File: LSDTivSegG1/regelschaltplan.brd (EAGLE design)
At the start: 160 x 100 mm, 48 parts, among them IC3 MAX232, IC4 MEGA32-P, Q2 BSS101, Q3 BSS101, Q4 BSS101, Q5 BSS101, Q6 BSS101, Q7 BSS101, Q8 BSS101, Q9 BSS101

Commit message: edit new schaltplan
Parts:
- removed IC3/7803: (no value), v-reg:78XXS
- added C12, C13, C14, C15, C16, C17: 100n, rcl:C025-025X050
- added IC1: LF33AB, lsd2016:TO220
- added JP1: (no value), jumper:JP1
- added R10: 10K, rcl:0207/7
- added R11: 10k, rcl:0207/7
- added R12, R13, R14: 240, rcl:0207/7
- added SJ1, SJ2, SJ3, SJ4, SJ5, SJ6, SJ7, SJ8: (no value), jumper:SJ
- added SV1: (no value), con-lstb:MA05-2
- C1, C2: value (none) -> 15p
- C10, C11, C8, C9: value (none) -> 1u
- C3, C4, C6, C7: value (none) -> 100n
- C5: value (none) -> 1000u
- R1, R2, R3, R4, R5, R6, R7, R8: value (none) -> 240; device rcl:0204/7 -> rcl:0207/7
- R9: value (none) -> 10K; device rcl:0204/7 -> rcl:0207/7
- moved R5 346.2 mm to (-17.8, -426.7)
- moved R1 346.2 mm to (-17.8, -406.4)
- moved R2 346.2 mm to (-17.8, -411.5)
- moved R3 346.2 mm to (-17.8, -416.6)
- moved R4 346.2 mm to (-17.8, -421.6)
- moved R6 346.2 mm to (-17.8, -431.8)
- moved R7 346.2 mm to (-17.8, -436.9)
- moved R8 346.2 mm to (-17.8, -442.0)
- moved R9 275.3 mm to (-17.8, -467.4)
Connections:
- new net ACCEL_X: C16.1, IC4.36, U$3.3
- new net ACCEL_Y: C17.1, IC4.37, U$3.5
- new net FOOT_SW_B: IC4.29, R11.2, U$2.5
- new net GYRO_REF: C15.1, IC4.35, U$3.11
- new net GYRO_X: C13.1, IC4.33, U$3.13
- new net GYRO_Y: C14.1, IC4.34, U$3.9
- new net MISO: IC4.7, SV1.9
- new net MOSI: IC4.6, SV1.1
- new net N$19: Q9.3, SJ8.1
- new net N$30: Q8.3, SJ7.1
- new net N$31: Q7.3, SJ6.1
- new net N$34: Q4.3, SJ3.1
- new net N$35: Q3.3, SJ2.1
- new net N$45: JP1.2, X1.9
- new net N$46: LED1.K, R3.1
- new net N$47: C5.1, IC4.21, R10.1
- new net POTI: C12.1, IC4.39, U$2.2
- new net RESET: C6.2, IC4.9, R9.2, SV1.5
- new net SCK: IC4.8, SV1.7
- new net STATUS_LED1: IC4.2, LED1.A
- new net STATUS_LED2: IC4.3, LED2.A
- new net STATUS_LED3: IC4.4, LED3.A
- net +3V3: now also IC1.3, Q9.2; no longer IC3/7803.OUT
- net +5V: now also IC1.1, JP1.1, Q8.2, SJ1.2, SJ2.2, SJ3.2, SJ4.2, SJ5.2, SJ6.2, SJ7.2, SJ8.2, SV1.2; no longer IC3/7803.IN, Q2.3, Q3.3, Q4.3, Q5.3, Q6.3, Q7.3, Q8.3, Q9.3, X1.9
- net BAT_PWM: now also Q7.2, R10.2
- net DIROUT_1: now also IC4.20, Q4.2
- net DIROUT_2: now also IC4.17, Q5.2
- net ENABLE: now also IC4.24, IC4.26, Q6.2
- net GND: now also C12.2, C13.2, C14.2, C15.2, C16.2, C17.2, C5.2, IC1.2, R1.2, R11.1, R12.2, R13.2, R14.2, R2.2, R3.2, R4.2, R5.2, R6.2, R7.2, R8.2, SV1.10, SV1.4, SV1.6, SV1.8; no longer IC3/7803.GND, LED1.K, LED2.K, LED3.K, R1.1, R2.1, R3.1, R4.1, R5.1, R6.1, R7.1, R8.1
- net MOTOR_PWM1: now also IC4.19, Q2.2
- net MOTOR_PWM2: now also IC4.18, Q3.2
- net N$10: now also R5.1; no longer R2.2
- net N$11: now also R6.1; no longer R3.2
- net N$14: now also R7.1; no longer R4.2
- net N$15: now also R8.1; no longer R5.2
- net N$16: now also R12.1; no longer R6.2
- net N$17: now also R13.1; no longer R7.2
- net N$18: now also R14.1; no longer R8.2
- net N$28: now also LED2.K, R2.1; no longer U$2.5
- net N$29: now also LED3.K, R1.1; no longer U$2.2
- net N$32: now also Q6.3, SJ5.1; no longer X1.3
- net N$33: now also Q5.3, SJ4.1; no longer X1.4
- net N$4: now also Q2.3, SJ1.1; no longer C6.2, IC4.9
- net N$7: now also R4.1; no longer R1.2
- net RS232RX: now also X1.3
- net RS232TX: now also X1.4

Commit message: merge commit (maybe layout)
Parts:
- moved R14 569.9 mm to (127.0, 94.0), turned to 90 degrees
- moved R13 563.7 mm to (121.9, 94.0), turned to 90 degrees
- moved R12 557.5 mm to (116.8, 94.0), turned to 90 degrees
- moved R8 551.4 mm to (111.8, 94.0), turned to 90 degrees
- moved R7 545.3 mm to (106.7, 94.0), turned to 90 degrees
- moved R6 539.2 mm to (101.6, 94.0), turned to 90 degrees
- moved R5 533.1 mm to (96.5, 94.0), turned to 90 degrees
- moved R4 527.1 mm to (91.4, 94.0), turned to 90 degrees
- moved R3 519.1 mm to (76.2, 94.0), turned to 90 degrees
- moved R2 515.1 mm to (81.3, 94.0), turned to 90 degrees
- moved R1 511.1 mm to (86.4, 94.0), turned to 90 degrees
- moved R10 505.9 mm to (116.8, 15.2)
- moved R9 505.9 mm to (116.8, 20.3)
- moved R11 505.9 mm to (116.8, 25.4)
- moved JP1 463.8 mm to (40.6, 81.3), turned to 90 degrees
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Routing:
- added copper zone on layer 16, net GND

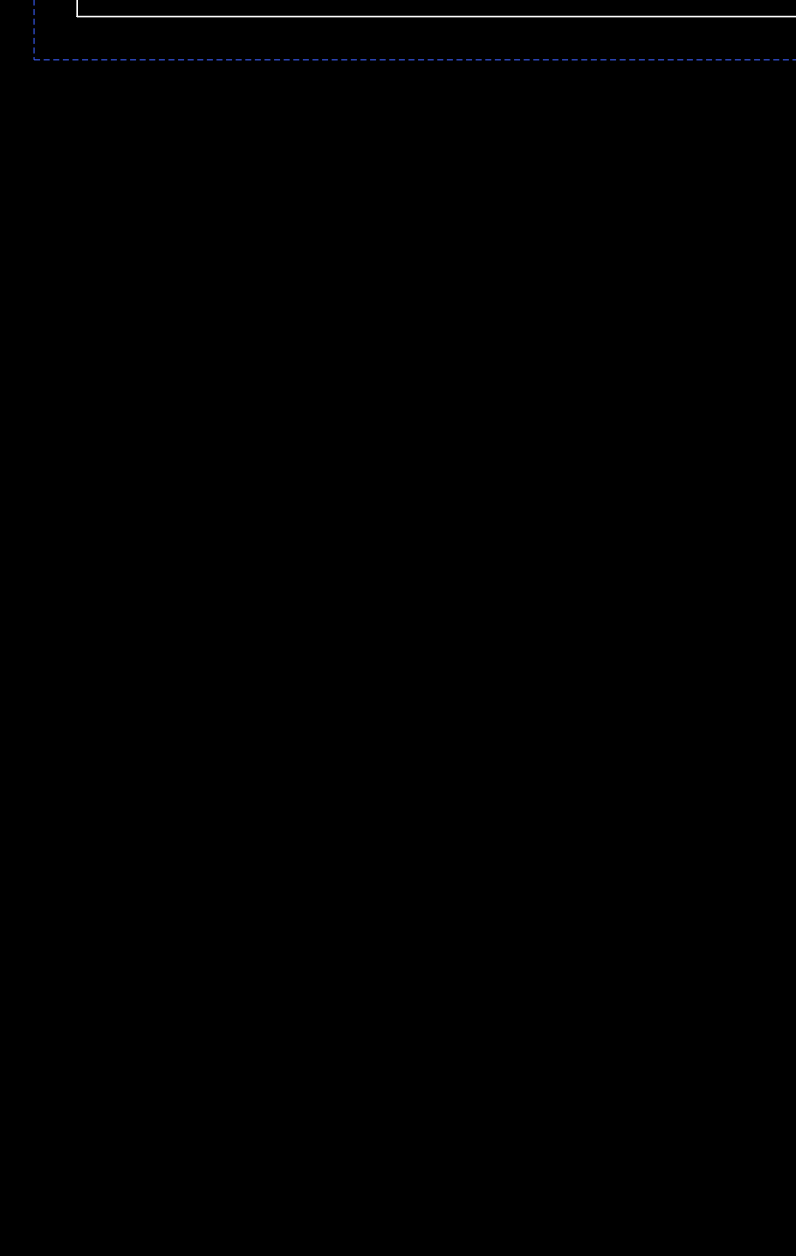
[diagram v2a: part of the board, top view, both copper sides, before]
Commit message: moved decoupling to regelungsplatine
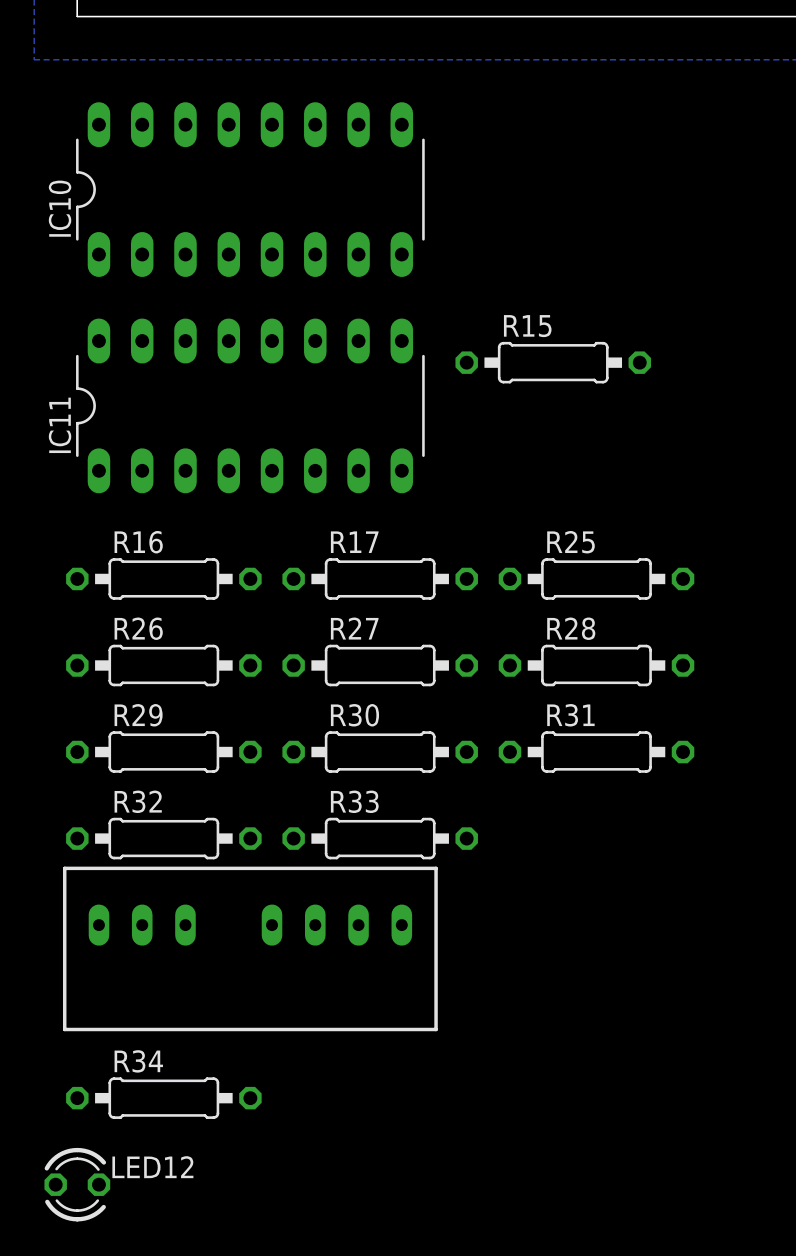
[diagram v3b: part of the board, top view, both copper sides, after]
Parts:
- added DC1: TMR, traco_tmr:TRACO_SIP-8
- added IC10, IC11: LTV844, lsd2016:DIL16
- added LED12: blau, led:LED3MM
- added R15, R16, R17, R25, R26, R27: 220, rcl:0207/10
- added R28, R29, R30, R31, R32, R33: 10k, rcl:0207/10
- added R34: 100, rcl:0207/10
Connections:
- net N$13 renamed NC
- removed net BAT_PWM: LEISTUNG.6, Q7.2, R10.2
- removed net DIROUT_1: IC4.20, LEISTUNG.5, Q4.2
- removed net DIROUT_2: IC4.17, LEISTUNG.7, Q5.2
- removed net ENABLE: IC4.24, IC4.26, LEISTUNG.9, Q6.2
- removed net MOTOR_PWM1: IC4.19, LEISTUNG.2, Q2.2
- removed net MOTOR_PWM2: IC4.18, LEISTUNG.4, Q3.2
- removed net N$12: LEISTUNG.8
- new net +24V: DC1.2, LEISTUNG.1
- new net 5V_LST: LEISTUNG.8, R28.1, R29.1, R30.1, R32.1, R33.1
- new net BAT_-: DC1.1, IC10.11, IC10.13, IC10.15, IC10.8, IC11.13, IC11.15, LEISTUNG.3
- new net BAT_PWM_CTL: IC10.10, Q7.2, R10.2, R31.2
- new net BAT_PWM_LST: LEISTUNG.6, R25.1
- new net DIRL_CTL: IC4.20, Q4.2, R15.1
- new net DIRL_LST: IC10.16, LEISTUNG.5, R28.2
- new net DIRR_CTL: IC4.17, Q5.2, R16.1
- new net DIRR_LST: IC10.14, LEISTUNG.7, R29.2
- new net ENABLE_CTL: IC4.24, IC4.26, Q6.2, R17.1
- new net ENABLE_LST: IC10.12, LEISTUNG.9, R30.2
- new net MOTOR_PWM_LST: LEISTUNG.2, LEISTUNG.4
- new net MOTOR_PWM_L_CTL: IC4.19, Q2.2, R26.1
- new net MOTOR_PWM_L_LST: IC11.16, R32.2
- new net MOTOR_PWM_R_CTL: IC4.18, Q3.2, R27.1
- new net MOTOR_PWM_R_LST: IC11.14, R33.2
- new net N$36: IC10.1, R15.2
- new net N$37: IC10.3, R16.2
- new net N$38: IC10.5, R17.2
- new net N$39: IC10.7, R25.2
- new net N$40: IC11.3, R27.2
- new net N$41: IC11.1, R26.2
- new net N$42: LED12.A, R34.1
- net +5V: now also DC1.6, R31.1, R34.2; no longer LEISTUNG.1
- net GND: now also C11.+, DC1.7, IC10.2, IC10.4, IC10.6, IC10.9, IC11.2, IC11.4, LED12.K; no longer C11.-, LEISTUNG.3
- net N$9: now also C11.-; no longer C11.+

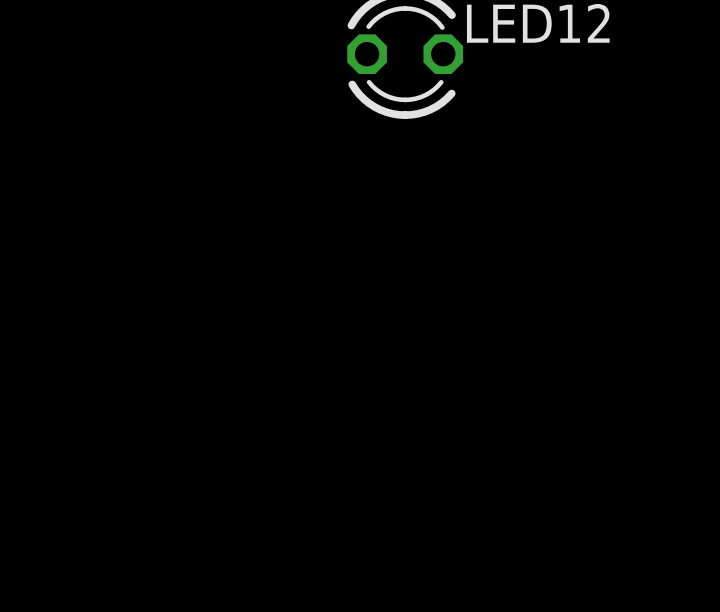
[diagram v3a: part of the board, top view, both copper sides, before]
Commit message: added blocking capacitors to 3V3 supply added rs323 cross pinhead
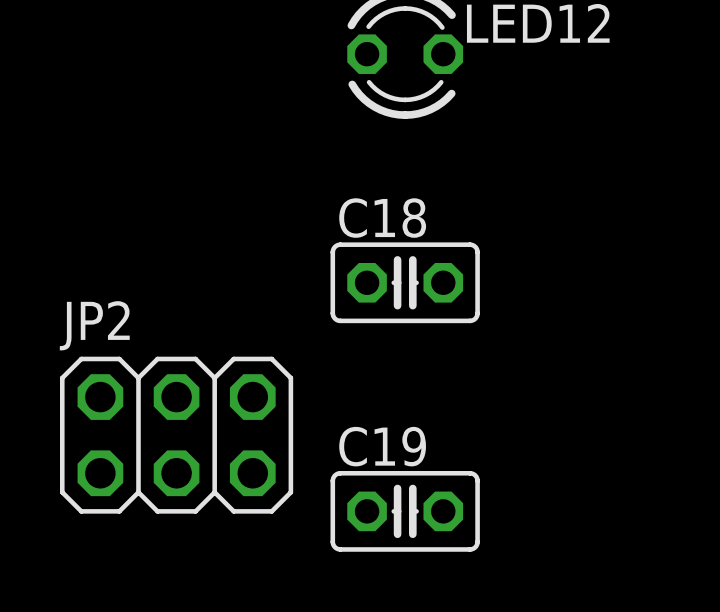
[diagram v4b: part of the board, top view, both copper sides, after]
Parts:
- added C18, C19: 100n, rcl:C025-025X050
- added JP2: (no value), pinhead:2X03
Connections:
- new net RS232RX_CON: JP2.3, X1.3
- new net RS232TX_CON: JP2.4, X1.4
- net +3V3: now also C19.1
- net +5V: now also C18.1
- net GND: now also C18.2, C19.2
- net RS232RX: now also JP2.1, JP2.6; no longer X1.3
- net RS232TX: now also JP2.2, JP2.5; no longer X1.4
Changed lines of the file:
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@@
 <element name="LED12" library="led" package="LED3MM" value="blau" x="0" y="-68.58"/>
 <element name="R34" library="rcl" package="0207/10" value="100" x="5.08" y="-63.5"/>
+<element name="C18" library="rcl" package="C025-025X050" value="100n" x="0" y="-76.2"/>
+<element name="C19" library="rcl" package="C025-025X050" value="100n" x="0" y="-83.82"/>
+<element name="JP2" library="pinhead" library_urn="urn:adsk.eagle:library:325" package="2X03" package3d_urn="urn:adsk.eagle:package:22462/2" value="" x="-7.62" y="-81.28"/>
 </elements>
 <signals>
@@
 <contactref element="IC11" pad="4"/>
 <contactref element="C11" pad="+"/>
+<contactref element="C18" pad="2"/>
+<contactref element="C19" pad="2"/>
 <wire x1="121.92" y1="97.79" x2="127" y2="97.79" width="0" layer="19" extent="1-1"/>
 <wire x1="116.84" y1="97.79" x2="121.92" y2="97.79" width="0" layer="19" extent="1-1"/>
@@
 <wire x1="16.51" y1="-53.34" x2="8.89" y2="-26.67" width="0" layer="19" extent="1-1"/>
 <wire x1="1.27" y1="-68.58" x2="16.51" y2="-53.34" width="0" layer="19" extent="1-1"/>
+<wire x1="1.27" y1="-76.2" x2="1.27" y2="-68.58" width="0" layer="19" extent="1-1"/>
+<wire x1="1.27" y1="-83.82" x2="1.27" y2="-76.2" width="0" layer="19" extent="1-1"/>
 </signal>
 <signal name="+3V3">
@@
 <contactref element="IC1" pad="3"/>
 <contactref element="Q9" pad="2"/>
+<contactref element="C19" pad="1"/>
 <wire x1="125.095" y1="76.2" x2="146.05" y2="65.278" width="0" layer="19" extent="1-1"/>
 <wire x1="146.05" y1="35.56" x2="146.05" y2="65.278" width="0" layer="19" extent="1-1"/>
@@
 <wire x1="82.55" y1="48.26" x2="125.095" y2="76.2" width="0" layer="19" extent="1-1"/>
 <wire x1="36.83" y1="7.62" x2="82.55" y2="48.26" width="0" layer="19" extent="1-1"/>
+<wire x1="-1.27" y1="-83.82" x2="36.83" y2="7.62" width="0" layer="19" extent="1-1"/>
 </signal>
 <signal name="VCC">
@@
 <contactref element="R34" pad="2"/>
 <contactref element="R31" pad="1"/>
+<contactref element="C18" pad="1"/>
 <wire x1="127" y1="69.342" x2="146.05" y2="62.738" width="0" layer="19" extent="1-1"/>
 <wire x1="121.92" y1="69.342" x2="127" y2="69.342" width="0" layer="19" extent="1-1"/>
@@
 <wire x1="13.97" y1="-53.34" x2="25.4" y2="-43.18" width="0" layer="19" extent="1-1"/>
 <wire x1="10.16" y1="-63.5" x2="13.97" y2="-53.34" width="0" layer="19" extent="1-1"/>
+<wire x1="-1.27" y1="-76.2" x2="10.16" y2="-63.5" width="0" layer="19" extent="1-1"/>
 </signal>
 <signal name="N$1">
@@
 <signal name="RS232RX">
 <contactref element="IC3" pad="14"/>
-<contactref element="X1" pad="3"/>
-<wire x1="31.75" y1="77.47" x2="28.448" y2="86.868" width="0" layer="19" extent="1-1"/>
+<contactref element="JP2" pad="6"/>
+<contactref element="JP2" pad="1"/>
+<wire x1="-5.08" y1="-80.01" x2="31.75" y2="77.47" width="0" layer="19" extent="1-1"/>
+<wire x1="-10.16" y1="-82.55" x2="-5.08" y2="-80.01" width="0" layer="19" extent="1-1"/>
 </signal>
 <signal name="RS232TX">
 <contactref element="IC3" pad="13"/>
-<contactref element="X1" pad="4"/>
-<wire x1="34.29" y1="77.47" x2="31.1912" y2="86.868" width="0" layer="19" extent="1-1"/>
+<contactref element="JP2" pad="2"/>
+<contactref element="JP2" pad="5"/>
+<wire x1="-10.16" y1="-80.01" x2="34.29" y2="77.47" width="0" layer="19" extent="1-1"/>
+<wire x1="-5.08" y1="-82.55" x2="-10.16" y2="-80.01" width="0" layer="19" extent="1-1"/>
 </signal>
 <signal name="N$7">
@@
 <wire x1="0" y1="-38.1" x2="107.95" y2="33.02" width="0" layer="19" extent="1-1"/>
 </signal>
+<signal name="RS232TX_CON">
+<contactref element="JP2" pad="4"/>
+<contactref element="X1" pad="4"/>
+<wire x1="-7.62" y1="-80.01" x2="31.1912" y2="86.868" width="0" layer="19" extent="1-1"/>
+</signal>
+<signal name="RS232RX_CON">
+<contactref element="JP2" pad="3"/>
+<contactref element="X1" pad="3"/>
+<wire x1="-7.62" y1="-82.55" x2="28.448" y2="86.868" width="0" layer="19" extent="1-1"/>
+</signal>
 </signals>
 <mfgpreviewcolors>
@@
 </board>
 </drawing>
+<compatibility>
+<note version="8.2" severity="warning">
+Since Version 8.2, EAGLE supports online libraries. The ids
+of those online libraries will not be understood (or retained)
+with this version.
+</note>
+<note version="8.3" severity="warning">
+Since Version 8.3, EAGLE supports URNs for individual library
+assets (packages, symbols, and devices). The URNs of those assets
+will not be understood (or retained) with this version.
+</note>
+<note version="8.3" severity="warning">
+Since Version 8.3, EAGLE supports the association of 3D packages
+with devices in libraries, schematics, and board files. Those 3D
+packages will not be understood (or retained) with this version.
+</note>
+</compatibility>
 </eagle>
